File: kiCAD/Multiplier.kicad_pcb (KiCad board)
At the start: 2 copper layers, 59.9 x 30 mm, 58 parts, among them IC2 ADG1221BRMZ, J1 Conn_01x02_Pin, J2 Conn_01x02_Pin, J3 Conn_01x02_Pin, Q7 Q_Dual_PNP_PNP_C1B1B2C2E2E1, Q8 Q_Dual_PNP_PNP_C1B1B2C2E2E1, U1 TS912, U10 TPS63060, U2 TLV340, U4 TS912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

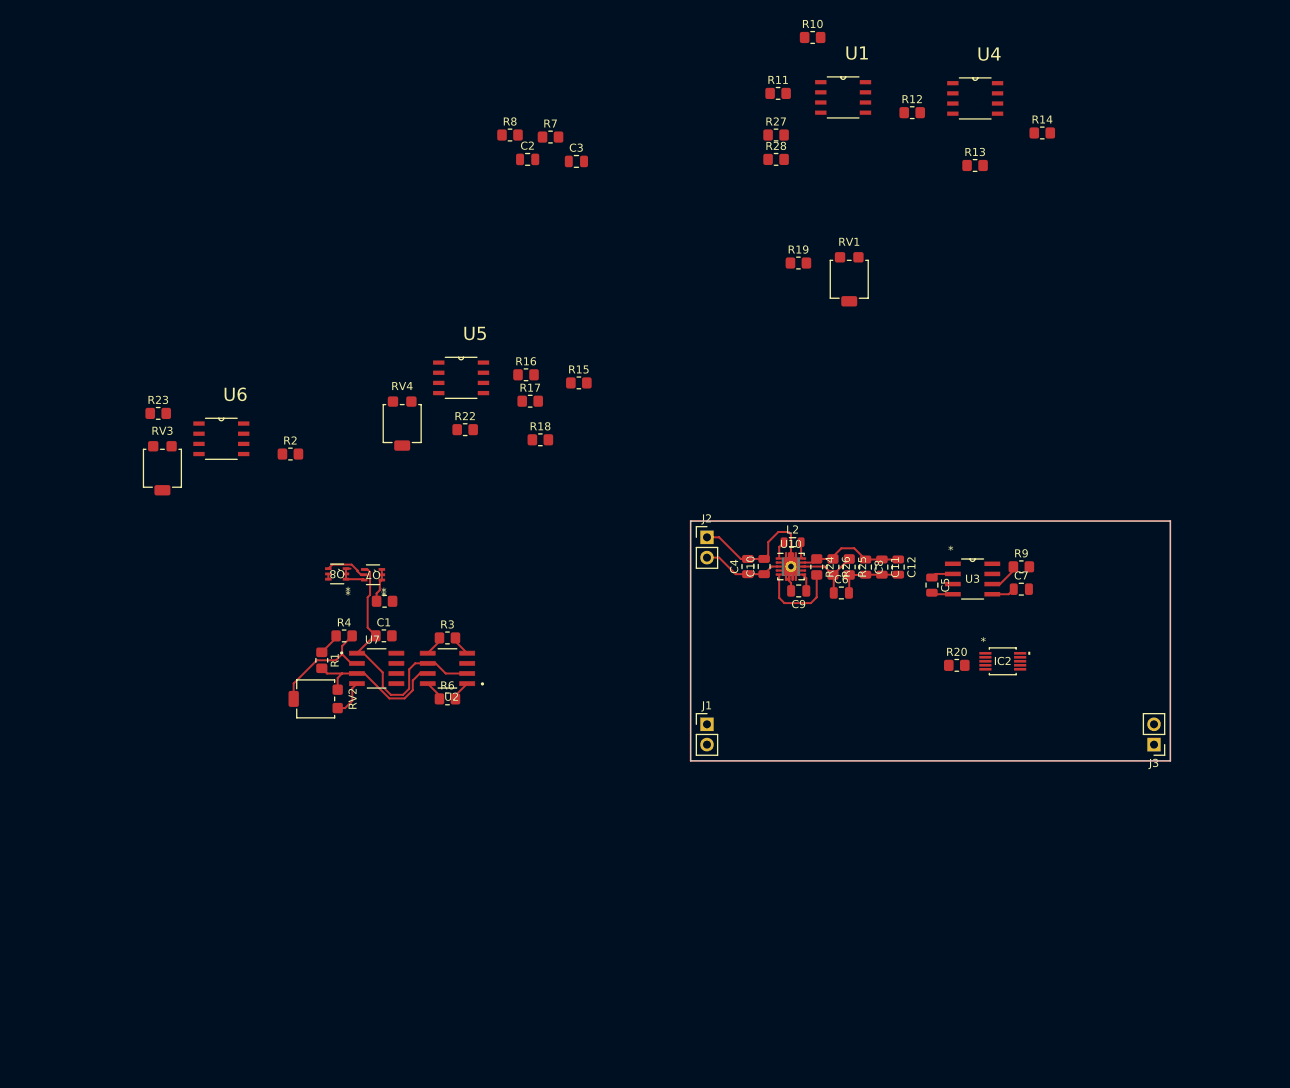
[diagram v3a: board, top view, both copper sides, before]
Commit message: First PCB design with GND fields and tantalum (100nF) coupling capacitor added
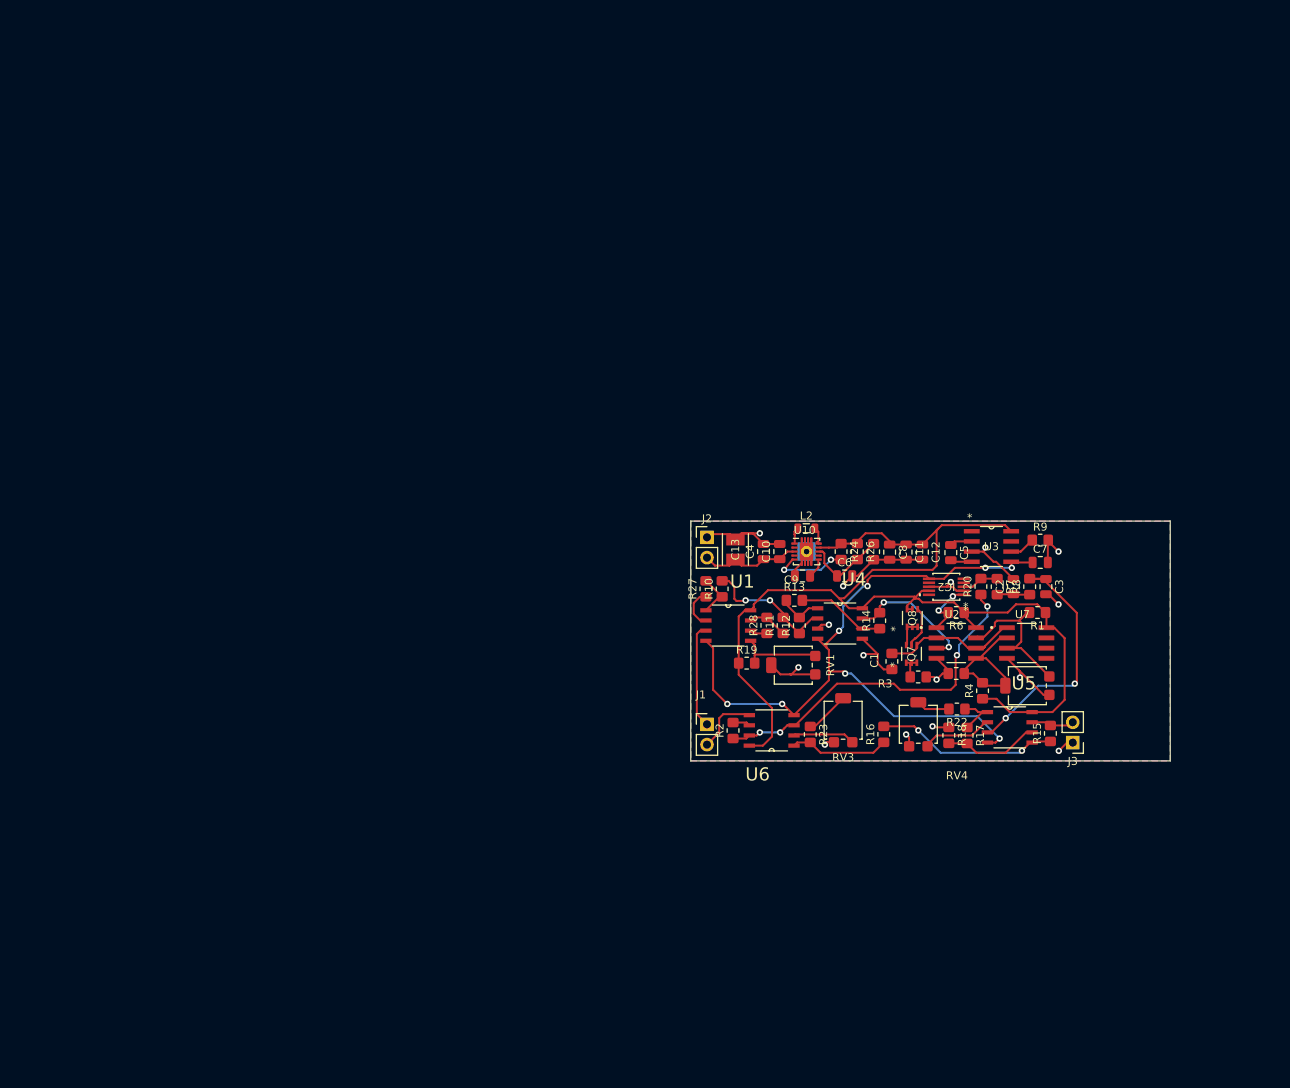
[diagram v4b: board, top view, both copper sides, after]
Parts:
- added C13: 100n, Custom:CAP_293D-B_VSS, F.Cu at (147.8, 84.3)
- moved R23 90.9 mm to (157.2, 107.4), turned to -90 degrees
- moved RV3 90.7 mm to (161.3, 105.7), turned to 180 degrees
- moved R1 89.7 mm to (185.6, 92.2), turned to 180 degrees
- moved RV2 89.0 mm to (184.3, 101.3)
- moved R8 86.1 mm to (184.6, 89.0), turned to 90 degrees
- moved U7 81.3 mm to (184.2, 96.0)
- moved U5 81.3 mm to (182.1, 106.6)
- moved C2 80.9 mm to (182.6, 89.0), turned to 90 degrees
- moved R4 80.1 mm to (178.7, 102.0), turned to 90 degrees
- moved R7 79.2 mm to (180.5, 89.0), turned to -90 degrees
- moved C3 79.2 mm to (186.6, 89.0), turned to -90 degrees
- moved U6 77.8 mm to (152.4, 106.9), turned to 180 degrees
- moved RV4 74.7 mm to (170.7, 106.2), turned to 180 degrees
- moved R15 73.4 mm to (187.2, 107.3), turned to 90 degrees
- moved Q8 72.1 mm to (169.9, 92.9), turned to 90 degrees
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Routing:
- net VCC: track 19.1 -> 139.9 mm
- net Vcc-: track 2.95 -> 90.1 mm, vias 0 -> 8
- net GND: track 35.7 -> 84.0 mm, vias 0 -> 15
- net Uy_buff: track 0.00 -> 44.5 mm, vias 0 -> 4
- net (UxUy + ErUy)/Asaw: track 0.00 -> 32.8 mm, vias 0 -> 2
- net Net-(U5B-+): track 0.00 -> 22.8 mm, vias 0 -> 2
- net Net-(U4A--): track 0.00 -> 17.1 mm, vias 0 -> 2
- net Ux+Er: track 0.00 -> 16.4 mm, vias 0 -> 2
- net Net-(Q7B-C2): track 33.2 -> 17.0 mm
- net Ux: track 0.00 -> 13.1 mm
- net UyEr: track 0.00 -> 12.5 mm
- net Net-(U4B--): track 0.00 -> 12.2 mm
- net Net-(U5B--): track 0.00 -> 12.0 mm
- net Er: track 0.00 -> 10.7 mm
- net Net-(U5A--): track 0.00 -> 8.86 mm
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- added copper zone on B.Cu, net GND
- added copper zone on F.Cu, net GND
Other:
- board text removed: "Adder"
- board text removed: "Buffered Er Ux"
- board text removed: "ER voltage div"
- board text removed: "RMS"
- board text removed: "curr_mirr"
- board text removed: "one quadrant mul"
- board text removed: "suctractor"

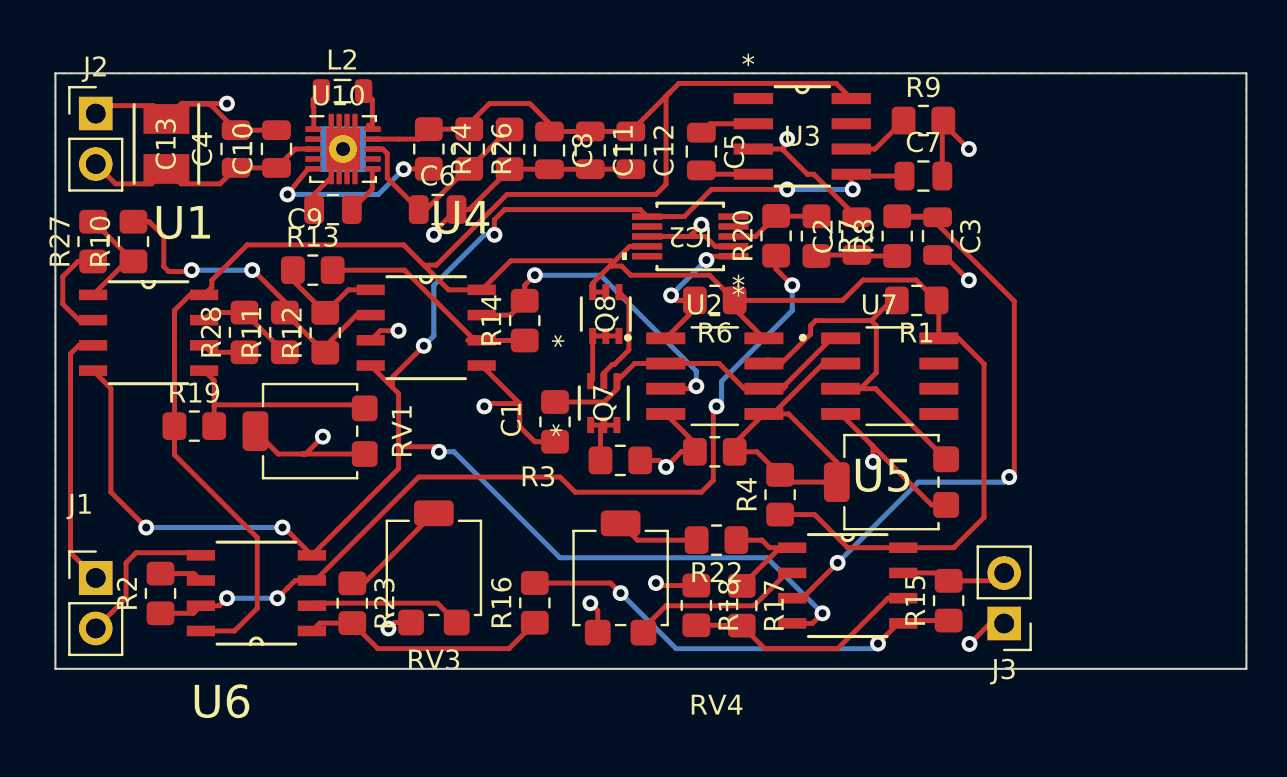
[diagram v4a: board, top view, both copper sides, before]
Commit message: Finished first PCB prototype
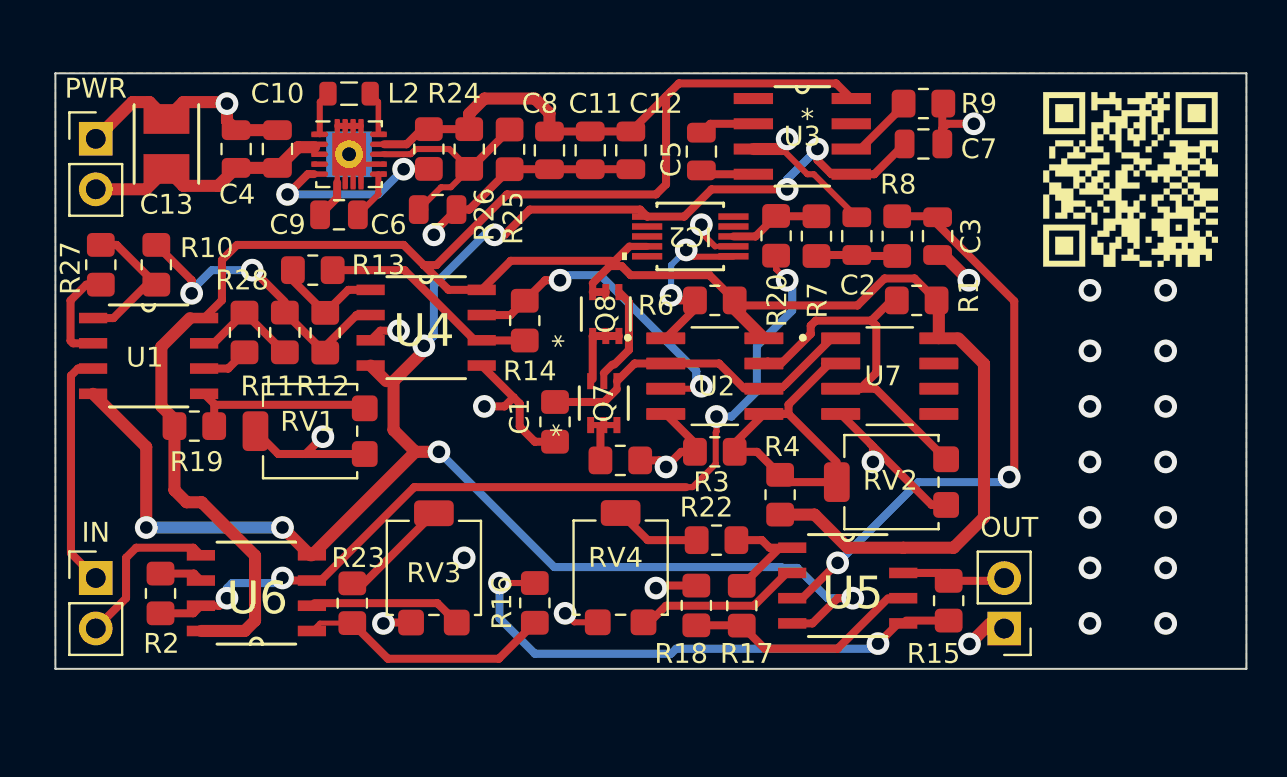
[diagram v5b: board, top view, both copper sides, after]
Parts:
- added G***: LOGO, Custom:tranzystory_yt_qr, F.Cu at (196.3, 86.1)
- moved R10 1.64 mm to (147.3, 90.4)
- moved C7 1.62 mm to (185.9, 84.3)
- moved PWR 1.27 mm to (144.3, 84.1)
- moved R27 1.23 mm to (144.5, 90.4)
- moved U1 1.17 mm to (146.9, 95.0)
- moved R9 0.85 mm to (185.9, 82.3)
- moved RV4 0.52 mm to (170.7, 105.7)
- moved C9 0.40 mm to (156.5, 87.9)
- moved U10 0.40 mm to (157.0, 84.8)
- moved L2 0.36 mm to (157.0, 81.8)
- moved OUT 0.25 mm to (190.0, 108.7)
- renumbered J1 to IN, J3 to OUT, J2 to PWR
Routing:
- net Net-(U5B-+): track 22.8 -> 27.6 mm
- net GND: track 84.0 -> 81.2 mm, vias 15 -> 30
- net Vcc-: track 90.1 -> 92.8 mm
- net VCC: track 139.9 -> 142.3 mm
- net (UxUy + ErUy)/Asaw: track 32.8 -> 30.6 mm
- net Net-(U10-FB): track 10.3 -> 12.4 mm
- net Net-(R10-Pad1): track 5.59 -> 7.53 mm
- net Er: track 10.7 -> 9.52 mm
- net Ux: track 13.1 -> 12.0 mm
- net Net-(U4A--): track 17.1 -> 16.0 mm
- net PWM_OUT: track 8.42 -> 9.22 mm
- net Net-(U4B--): track 12.2 -> 11.5 mm
- net Uy: track 7.96 -> 8.50 mm
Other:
- board text added: "MultiplierV1 by: Piotr Łetowski Michał Nizioł Michał Zelek"
- board text added: "R25"
- board text added: "RV2"
- board text added: "U1"

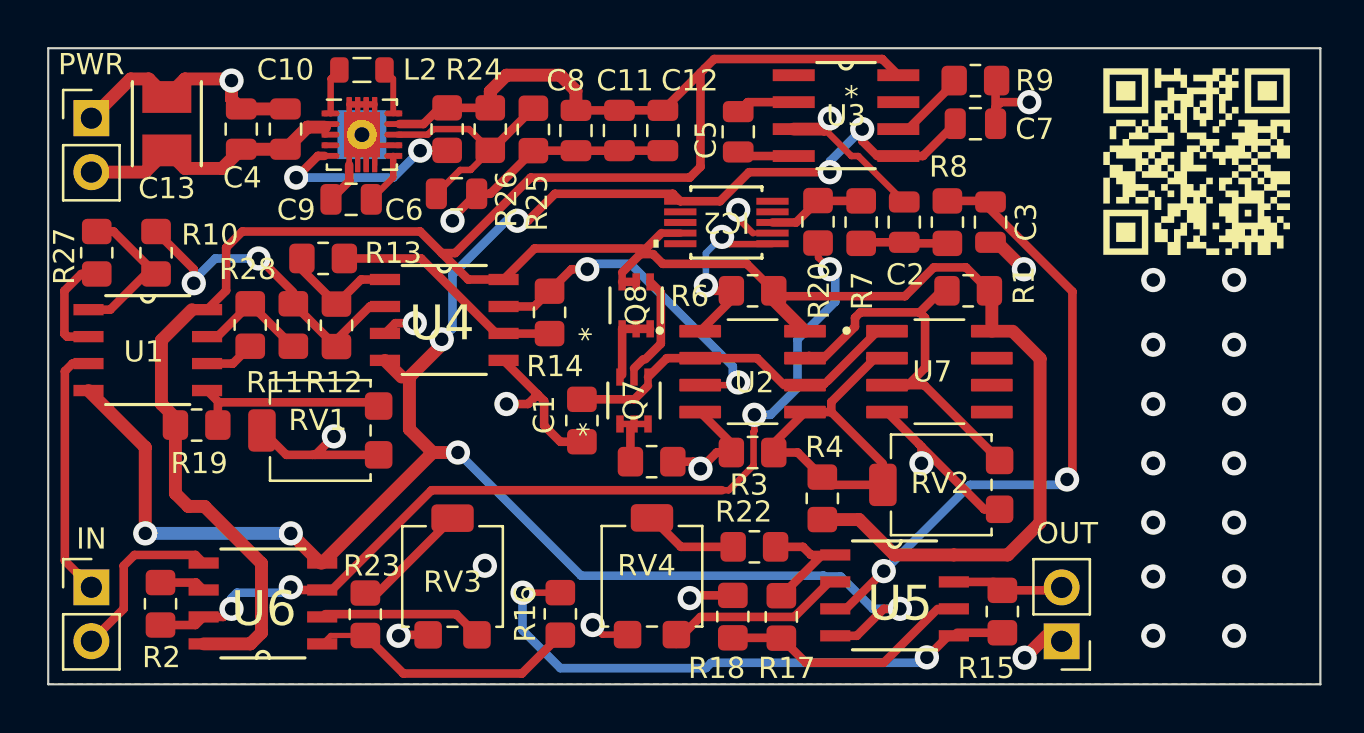
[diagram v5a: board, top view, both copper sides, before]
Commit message: New schematic image, final PCB design
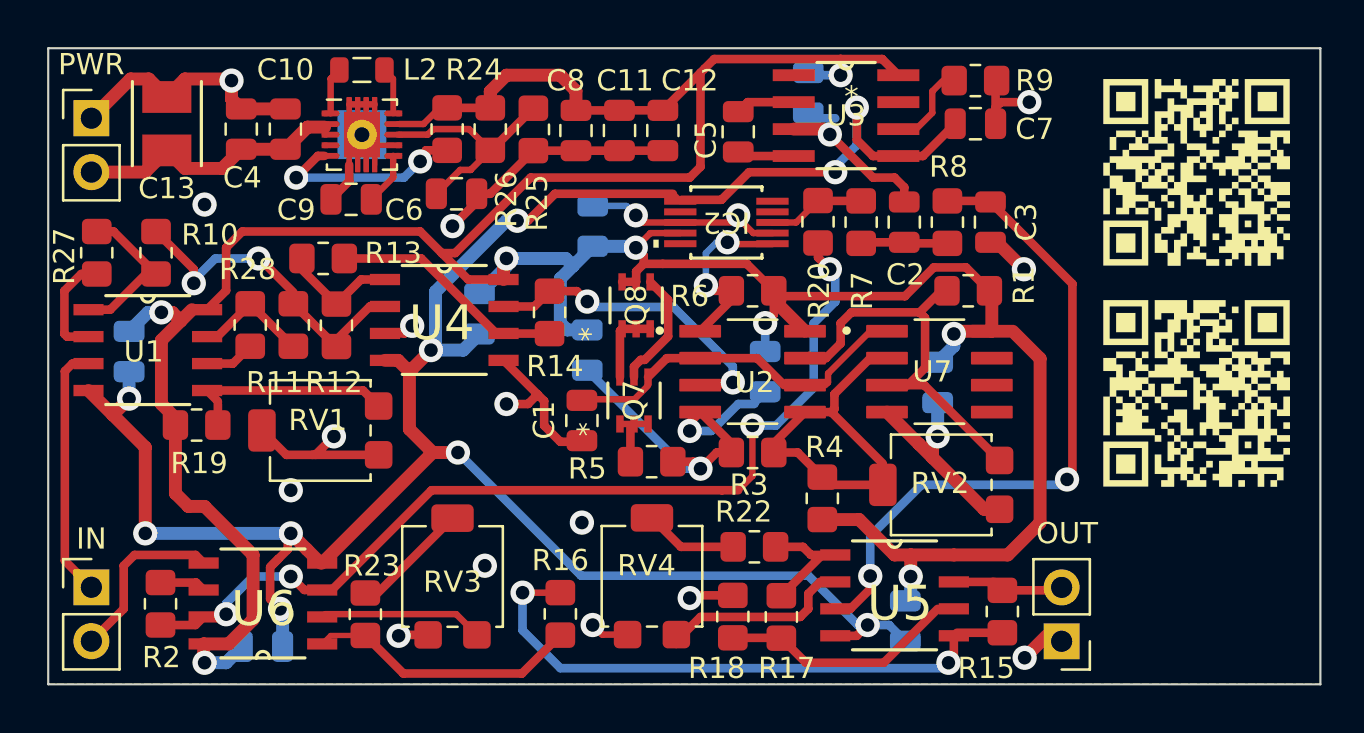
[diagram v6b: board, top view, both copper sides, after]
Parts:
- added C14: 100n, Capacitor_SMD:C_0805_2012Metric, B.Cu at (178.1, 82.9)
- added C15: 100n, Capacitor_SMD:C_0805_2012Metric, B.Cu at (167.9, 89.2)
- added C16: 100n, Capacitor_SMD:C_0805_2012Metric, B.Cu at (167.6, 95.0)
- added C17: 100n, Capacitor_SMD:C_0805_2012Metric, B.Cu at (152.3, 109.0)
- added C18: 100n, Capacitor_SMD:C_0805_2012Metric, B.Cu at (182.6, 107.8)
- added C19: 100n, Capacitor_SMD:C_0805_2012Metric, B.Cu at (162.6, 93.3)
- added C20: 100n, Capacitor_SMD:C_0805_2012Metric, B.Cu at (146.1, 95.1)
- added C21: 100n, Capacitor_SMD:C_0805_2012Metric, B.Cu at (176.0, 96.0)
- added C22: 100n, Capacitor_SMD:C_0805_2012Metric, B.Cu at (184.2, 96.5)
- added G***: LOGO, Custom:repo_qr, F.Cu at (196.3, 97.0)
- C1: footprint Resistor_SMD:R_0805_2012Metric_Pad1.20x1.40mm_HandSolder -> Capacitor_SMD:C_0805_2012Metric
- C13: value 100n -> 100u
- moved G*** 0.51 mm to (196.3, 86.6)
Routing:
- net VCC: track 142.3 -> 165.5 mm, vias 0 -> 8
- net GND: track 81.2 -> 104.1 mm, vias 30 -> 21
- net Vcc-: track 92.8 -> 105.4 mm, vias 8 -> 10
- net Ux+Er: track 16.5 -> 14.9 mm
- net (UxUy + ErUy)/Asaw: track 30.6 -> 31.8 mm
- net Net-(U7A-+): track 20.2 -> 21.3 mm
- net Er: track 9.52 -> 10.6 mm
- net Uy_buff: track 44.3 -> 45.3 mm
- net Net-(U5B-+): track 27.6 -> 28.4 mm
- net Net-(Q7B-E2): track 5.28 -> 6.03 mm
- net Net-(U5A--): track 8.73 -> 9.42 mm
- net Net-(U3-LV): track 3.65 -> 4.29 mm
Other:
- board text added: "R5"
